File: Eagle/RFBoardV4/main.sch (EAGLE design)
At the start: 31 parts, among them Q1 8/16/20MHz, U1 ATMEGA328

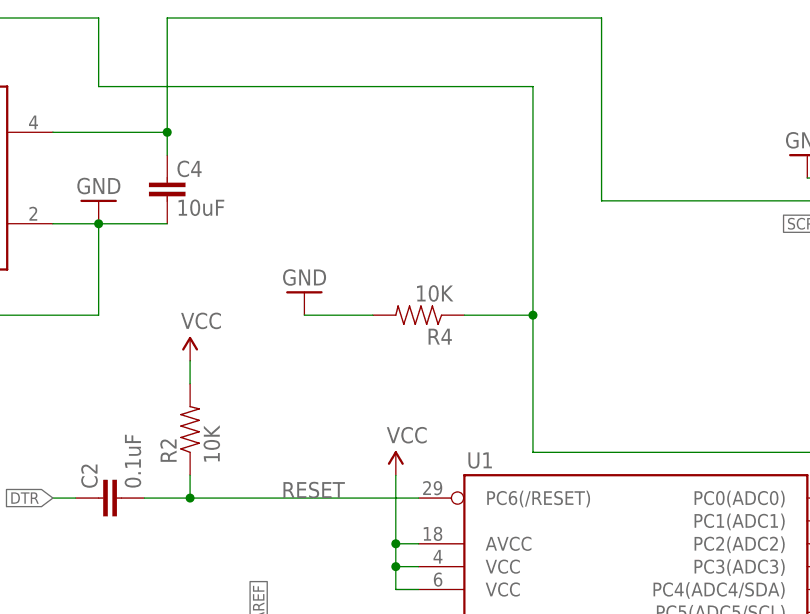
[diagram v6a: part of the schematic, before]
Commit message: Minor updates moving from 4.3 to 4.4
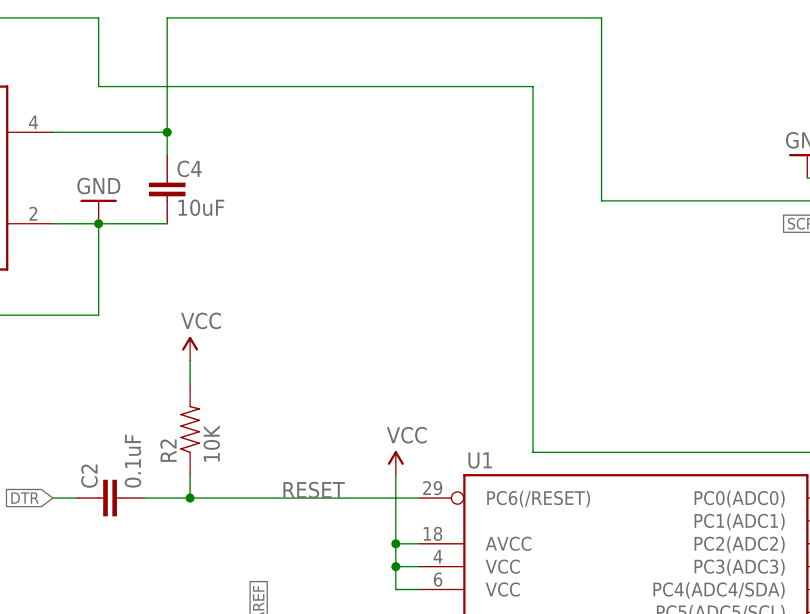
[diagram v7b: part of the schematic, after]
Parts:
- removed R4: 10K, SparkFun:RESISTOR0603-RES
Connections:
- net D5: no longer R4.1
- net GND: no longer R4.2
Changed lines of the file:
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@@
 <?xml version="1.0" encoding="utf-8"?>
 <!DOCTYPE eagle SYSTEM "eagle.dtd">
-<eagle version="7.5.0">
+<eagle version="7.2.0">
 <drawing>
 <settings>
@@
 <part name="JP4" library="SparkFun-Connectors" deviceset="M03" device="SCREW"/>
 <part name="GND10" library="SparkFun" deviceset="GND" device=""/>
-<part name="R4" library="SparkFun" deviceset="RESISTOR" device="0603-RES" value="10K"/>
-<part name="GND11" library="SparkFun" deviceset="GND" device=""/>
 <part name="U$1" library="battery_wilkie" deviceset="BAT" device=""/>
 <part name="P+6" library="SparkFun" deviceset="3.3V" device="" value="VCC"/>
@@
 <instance part="JP4" gate="G$1" x="220.98" y="187.96" rot="R180"/>
 <instance part="GND10" gate="1" x="190.5" y="193.04" rot="R180"/>
-<instance part="R4" gate="G$1" x="147.32" y="175.26" rot="R180"/>
-<instance part="GND11" gate="1" x="134.62" y="177.8" rot="R180"/>
 <instance part="U$1" gate="G$1" x="43.18" y="147.32"/>
 <instance part="P+6" gate="G$1" x="15.24" y="170.18"/>
@@
 </segment>
 <segment>
-<pinref part="R4" gate="G$1" pin="2"/>
-<pinref part="GND11" gate="1" pin="GND"/>
-<wire x1="142.24" y1="175.26" x2="134.62" y2="175.26" width="0.1524" layer="91"/>
-</segment>
-<segment>
 <pinref part="GND12" gate="1" pin="GND"/>
 <pinref part="U$1" gate="G$1" pin="GND"/>
@@
 <pinref part="U1" gate="G$1" pin="PD5(T1)"/>
 <wire x1="195.58" y1="119.38" x2="208.28" y2="119.38" width="0.1524" layer="91"/>
-<wire x1="160.02" y1="175.26" x2="160.02" y2="160.02" width="0.1524" layer="91"/>
 <wire x1="160.02" y1="160.02" x2="208.28" y2="160.02" width="0.1524" layer="91"/>
 <wire x1="208.28" y1="160.02" x2="208.28" y2="119.38" width="0.1524" layer="91"/>
-<pinref part="R4" gate="G$1" pin="1"/>
-<wire x1="152.4" y1="175.26" x2="160.02" y2="175.26" width="0.1524" layer="91"/>
-<junction x="160.02" y="175.26"/>
-<wire x1="160.02" y1="175.26" x2="160.02" y2="200.66" width="0.1524" layer="91"/>
+<wire x1="160.02" y1="160.02" x2="160.02" y2="200.66" width="0.1524" layer="91"/>
 <pinref part="U$2" gate="IC1" pin="CE"/>
 <wire x1="76.2" y1="190.5" x2="71.12" y2="190.5" width="0.1524" layer="91"/>

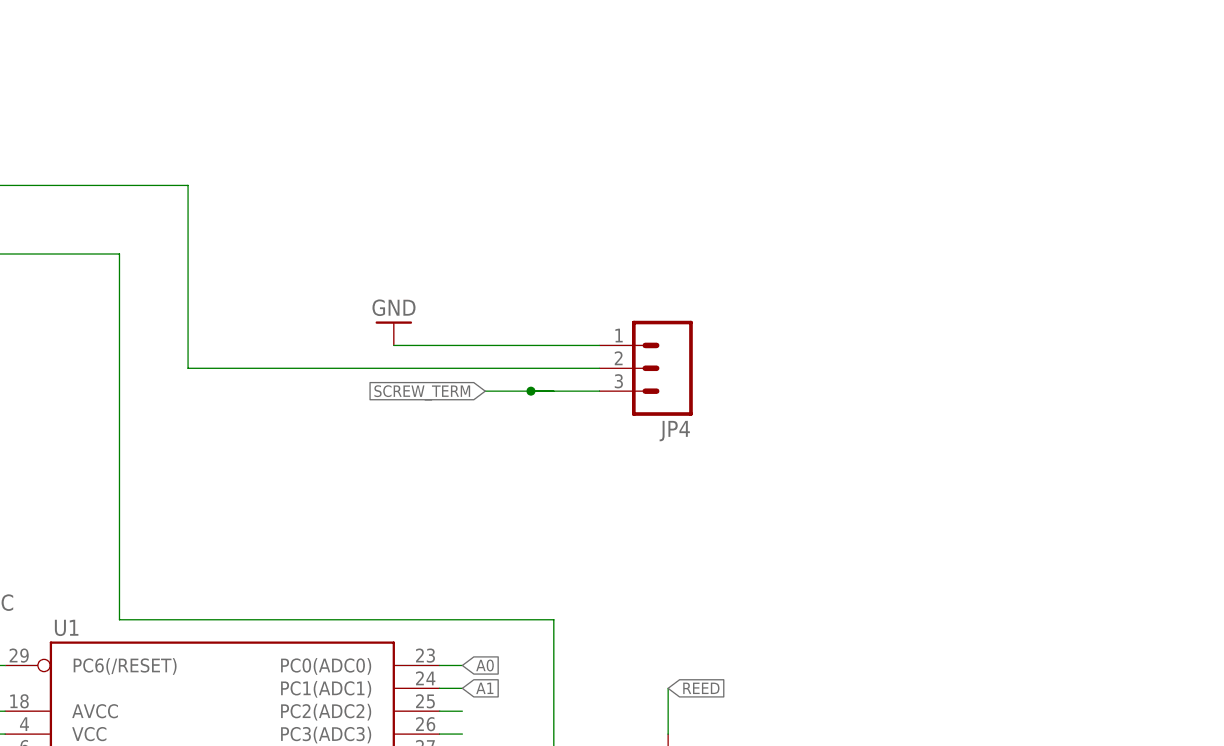
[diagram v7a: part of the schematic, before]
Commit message: Added external power option
- Added option for micro USB B for external power
- Added option for 3.3v linear regulator
- Added option for power input screw terminal
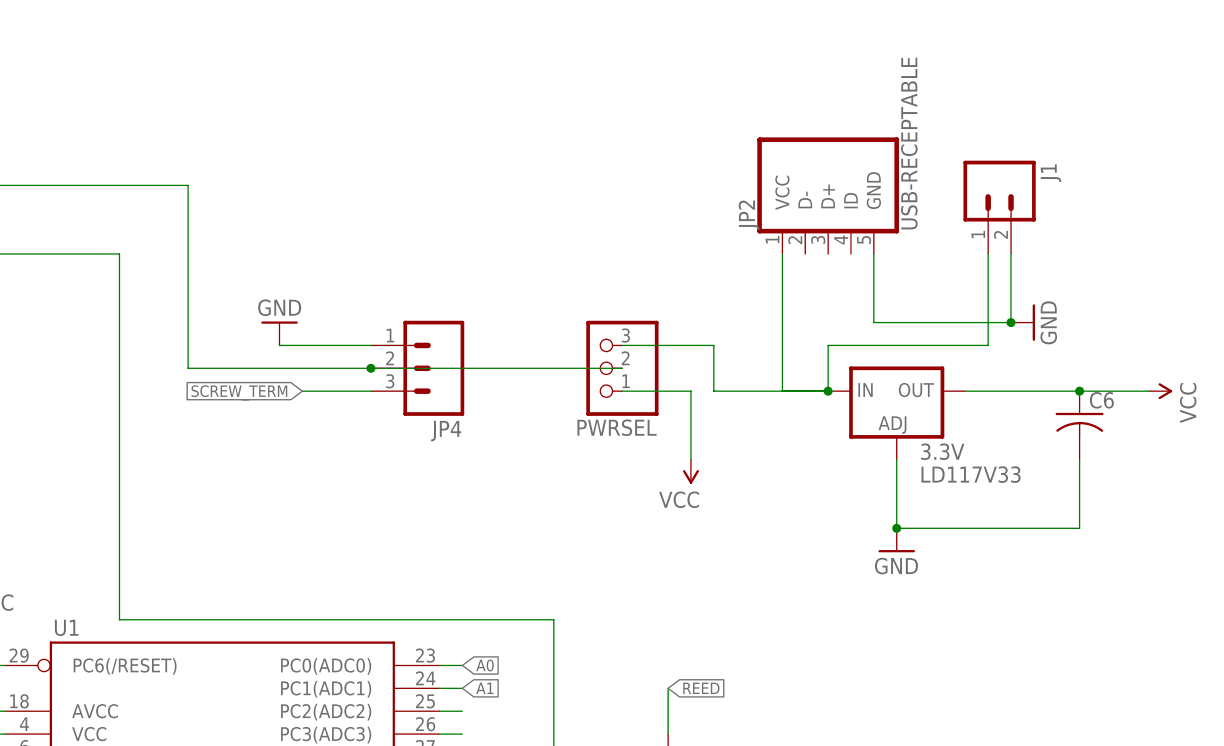
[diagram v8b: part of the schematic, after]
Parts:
- added 3.3V: LD117V33, v-reg:LD117AV
- added C6: (no value), rcl:C-US050-075X075
- added J1: (no value), SparkFun-Connectors:M023.5MM
- added JP2: USB-RECEPTABLE, daspilker:USB-RECEPTABLE
- added PWRSEL: (no value), pinhead:PINHD-1X3
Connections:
- new net 3.3V: 3.3V.OUT, C6.1, PWRSEL.1
- new net RAW_PWR: 3.3V.IN, J1.1, JP2.VCC, PWRSEL.3
- net GND: now also 3.3V.ADJ, C6.2, J1.2, JP2.GND
- net REG_3.3V: now also PWRSEL.2
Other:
- moved on the sheet: JP4
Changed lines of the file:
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@@
 <?xml version="1.0" encoding="utf-8"?>
 <!DOCTYPE eagle SYSTEM "eagle.dtd">
-<eagle version="7.2.0">
+<eagle version="7.1.0">
 <drawing>
 <settings>
@@
 <layer number="56" name="wert" color="7" fill="1" visible="no" active="no"/>
 <layer number="57" name="tCAD" color="7" fill="1" visible="no" active="no"/>
+<layer number="59" name="tCarbon" color="7" fill="1" visible="no" active="no"/>
+<layer number="60" name="bCarbon" color="7" fill="1" visible="no" active="no"/>
 <layer number="90" name="Modules" color="5" fill="1" visible="yes" active="yes"/>
 <layer number="91" name="Nets" color="2" fill="1" visible="yes" active="yes"/>
@@
 <layer number="127" name="_tValues" color="7" fill="1" visible="yes" active="yes"/>
 <layer number="128" name="_bValues" color="7" fill="1" visible="yes" active="yes"/>
+<layer number="129" name="Mask" color="7" fill="1" visible="yes" active="yes"/>
 <layer number="130" name="SMDSTROOK" color="7" fill="1" visible="yes" active="yes"/>
 <layer number="131" name="tAdjust" color="7" fill="1" visible="yes" active="yes"/>
@@
 <layer number="227" name="227bmp" color="7" fill="1" visible="no" active="yes"/>
 <layer number="228" name="228bmp" color="7" fill="1" visible="no" active="yes"/>
+<layer number="229" name="229bmp" color="7" fill="1" visible="yes" active="yes"/>
 <layer number="230" name="230bmp" color="7" fill="1" visible="no" active="yes"/>
 <layer number="231" name="Eagle3D_PG1" color="7" fill="1" visible="yes" active="yes"/>
@@
 <part name="GND14" library="SparkFun" deviceset="GND" device=""/>
 <part name="D7-D1" library="pinhead" deviceset="PINHD-1X2" device=""/>
+<part name="JP2" library="daspilker" deviceset="USB-RECEPTABLE" device=""/>
+<part name="3.3V" library="v-reg" deviceset="LD117A?*" device="V" value="LD117V33"/>
+<part name="J1" library="SparkFun-Connectors" deviceset="M02" device="3.5MM"/>
+<part name="C6" library="rcl" deviceset="C-US" device="050-075X075"/>
+<part name="GND3" library="SparkFun" deviceset="GND" device=""/>
+<part name="GND11" library="SparkFun" deviceset="GND" device=""/>
+<part name="P+5" library="SparkFun" deviceset="3.3V" device="" value="VCC"/>
+<part name="PWRSEL" library="pinhead" deviceset="PINHD-1X3" device=""/>
+<part name="P+8" library="SparkFun" deviceset="3.3V" device="" value="VCC"/>
 </parts>
 <sheets>
@@
 <instance part="GND9" gate="1" x="48.26" y="93.98"/>
 <instance part="R3" gate="G$1" x="30.48" y="106.68" rot="R90"/>
-<instance part="JP4" gate="G$1" x="220.98" y="187.96" rot="R180"/>
-<instance part="GND10" gate="1" x="190.5" y="193.04" rot="R180"/>
+<instance part="JP4" gate="G$1" x="195.58" y="187.96" rot="R180"/>
+<instance part="GND10" gate="1" x="177.8" y="193.04" rot="R180"/>
 <instance part="U$1" gate="G$1" x="43.18" y="147.32"/>
 <instance part="P+6" gate="G$1" x="15.24" y="170.18"/>
@@
 <instance part="GND14" gate="1" x="111.76" y="187.96" rot="R180"/>
 <instance part="D7-D1" gate="G$1" x="17.78" y="124.46" rot="R180"/>
+<instance part="JP2" gate="G$1" x="238.76" y="208.28" rot="R90"/>
+<instance part="3.3V" gate="G$1" x="246.38" y="185.42"/>
+<instance part="J1" gate="G$1" x="256.54" y="208.28" rot="R270"/>
+<instance part="C6" gate="G$1" x="266.7" y="182.88"/>
+<instance part="GND3" gate="1" x="261.62" y="193.04" rot="R90"/>
+<instance part="GND11" gate="1" x="246.38" y="167.64"/>
+<instance part="P+5" gate="G$1" x="274.32" y="185.42" rot="R270"/>
+<instance part="PWRSEL" gate="A" x="213.36" y="187.96" rot="R180"/>
+<instance part="P+8" gate="G$1" x="223.52" y="177.8" rot="R180"/>
 </instances>
 <busses>
@@
 <pinref part="JP4" gate="G$1" pin="1"/>
 <pinref part="GND10" gate="1" pin="GND"/>
-<wire x1="213.36" y1="190.5" x2="190.5" y2="190.5" width="0.1524" layer="91"/>
+<wire x1="187.96" y1="190.5" x2="177.8" y2="190.5" width="0.1524" layer="91"/>
+</segment>
+<segment>
+<pinref part="GND3" gate="1" pin="GND"/>
+<pinref part="J1" gate="G$1" pin="2"/>
+<wire x1="259.08" y1="193.04" x2="259.08" y2="200.66" width="0.1524" layer="91"/>
+<pinref part="JP2" gate="G$1" pin="GND"/>
+<wire x1="259.08" y1="193.04" x2="243.84" y2="193.04" width="0.1524" layer="91"/>
+<wire x1="243.84" y1="193.04" x2="243.84" y2="200.66" width="0.1524" layer="91"/>
+<junction x="259.08" y="193.04"/>
+</segment>
+<segment>
+<pinref part="GND11" gate="1" pin="GND"/>
+<pinref part="3.3V" gate="G$1" pin="ADJ"/>
+<wire x1="246.38" y1="170.18" x2="246.38" y2="177.8" width="0.1524" layer="91"/>
+<pinref part="C6" gate="G$1" pin="2"/>
+<wire x1="246.38" y1="170.18" x2="266.7" y2="170.18" width="0.1524" layer="91"/>
+<wire x1="266.7" y1="170.18" x2="266.7" y2="177.8" width="0.1524" layer="91"/>
+<junction x="246.38" y="170.18"/>
 </segment>
 </net>
@@
 <segment>
 <pinref part="JP4" gate="G$1" pin="3"/>
-<junction x="205.74" y="185.42"/>
-<wire x1="205.74" y1="185.42" x2="213.36" y2="185.42" width="0.1524" layer="91"/>
-<wire x1="205.74" y1="185.42" x2="208.28" y2="185.42" width="0.1524" layer="91"/>
-<wire x1="200.66" y1="185.42" x2="205.74" y2="185.42" width="0.1524" layer="91"/>
-<label x="200.66" y="185.42" size="1.27" layer="95" rot="R180" xref="yes"/>
+<wire x1="180.34" y1="185.42" x2="187.96" y2="185.42" width="0.1524" layer="91"/>
+<label x="180.34" y="185.42" size="1.27" layer="95" rot="R180" xref="yes"/>
 </segment>
 </net>
@@
 </segment>
 </net>
-<net name="REG_3.3V" class="0">
+<net name="REG_3.3V" class="1">
 <segment>
 <pinref part="U$2" gate="IC1" pin="VOUT"/>
@@
 <wire x1="167.64" y1="208.28" x2="167.64" y2="187.96" width="0.1524" layer="91"/>
 <pinref part="JP4" gate="G$1" pin="2"/>
-<wire x1="167.64" y1="187.96" x2="213.36" y2="187.96" width="0.1524" layer="91"/>
+<wire x1="167.64" y1="187.96" x2="187.96" y2="187.96" width="0.1524" layer="91"/>
 <pinref part="C4" gate="G$1" pin="2"/>
 <wire x1="119.38" y1="193.04" x2="119.38" y2="195.58" width="0.1524" layer="91"/>
 <junction x="119.38" y="195.58"/>
+<pinref part="PWRSEL" gate="A" pin="2"/>
+<wire x1="215.9" y1="187.96" x2="187.96" y2="187.96" width="0.1524" layer="91"/>
+<junction x="187.96" y="187.96"/>
 </segment>
 </net>
@@
 </segment>
 </net>
+<net name="RAW_PWR" class="1">
+<segment>
+<pinref part="3.3V" gate="G$1" pin="IN"/>
+<pinref part="JP2" gate="G$1" pin="VCC"/>
+<wire x1="238.76" y1="185.42" x2="233.68" y2="185.42" width="0.1524" layer="91"/>
+<wire x1="233.68" y1="185.42" x2="233.68" y2="200.66" width="0.1524" layer="91"/>
+<wire x1="238.76" y1="185.42" x2="238.76" y2="190.5" width="0.1524" layer="91"/>
+<junction x="238.76" y="185.42"/>
+<pinref part="J1" gate="G$1" pin="1"/>
+<wire x1="238.76" y1="190.5" x2="256.54" y2="190.5" width="0.1524" layer="91"/>
+<wire x1="256.54" y1="190.5" x2="256.54" y2="200.66" width="0.1524" layer="91"/>
+<wire x1="238.76" y1="185.42" x2="226.06" y2="185.42" width="0.1524" layer="91"/>
+<wire x1="226.06" y1="185.42" x2="226.06" y2="190.5" width="0.1524" layer="91"/>
+<pinref part="PWRSEL" gate="A" pin="3"/>
+<wire x1="226.06" y1="190.5" x2="215.9" y2="190.5" width="0.1524" layer="91"/>
+</segment>
+</net>
+<net name="3.3V" class="1">
+<segment>
+<pinref part="3.3V" gate="G$1" pin="OUT"/>
+<pinref part="C6" gate="G$1" pin="1"/>
+<wire x1="254" y1="185.42" x2="266.7" y2="185.42" width="0.1524" layer="91"/>
+<pinref part="P+5" gate="G$1" pin="3.3V"/>
+<wire x1="274.32" y1="185.42" x2="266.7" y2="185.42" width="0.1524" layer="91"/>
+<junction x="266.7" y="185.42"/>
+</segment>
+<segment>
+<pinref part="P+8" gate="G$1" pin="3.3V"/>
+<wire x1="223.52" y1="177.8" x2="223.52" y2="185.42" width="0.1524" layer="91"/>
+<pinref part="PWRSEL" gate="A" pin="1"/>
+<wire x1="223.52" y1="185.42" x2="215.9" y2="185.42" width="0.1524" layer="91"/>
+</segment>
+</net>
